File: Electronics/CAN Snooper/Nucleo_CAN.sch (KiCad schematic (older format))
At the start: 35 parts, among them J1 Car Power, J2 CAN Bus, SW1 Reset, T1 12V Iso Test, T10 CAN L Test, T11 CAN Output GND Test, T2 5V Iso Test, T3 9V Test, T4 3.3V Test, T5 CAN PwrSense Test, T6 CAN Tx Test, T7 CAN Rx Test, T8 CAN Input GND Test, T9 CAN H Test, U1 PDS1-S12-S9-M, U2 MCP1702T-5002E/CB, U3 Nucleo_L432KC, U4 ADM3054

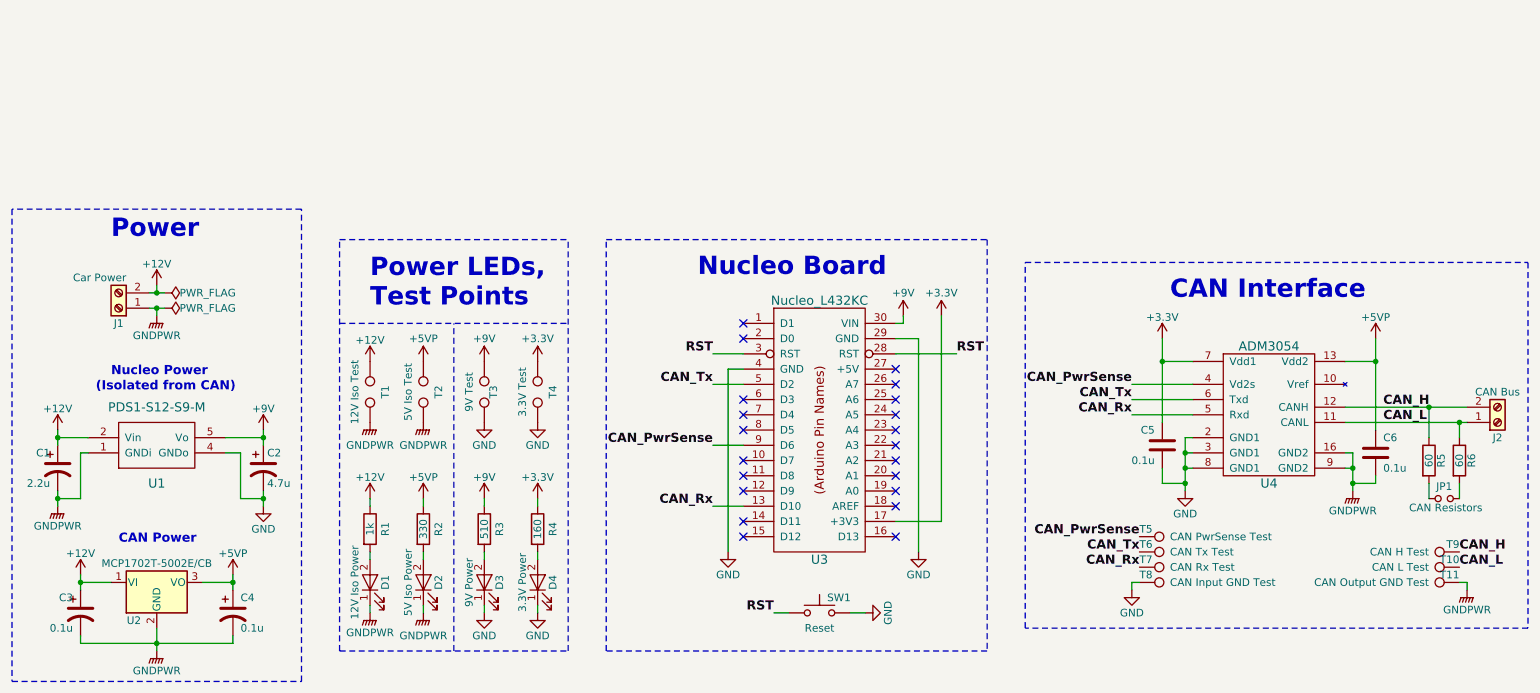
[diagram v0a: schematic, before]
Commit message: CAN Snooper: Schematic: Merge PWR and CAN connectors; bump rev.
In order to facilitate easy power and CAN connection, I've combined
the two into a single connector rather than two separate screw
terminals. Additionally, I've added a duplicate connector to make
chaining CAN connections simple, removing the need for splitters or
radial bus layouts.

I created a schematic symbol for our connector to make sure that we
use a consistent pinout across our designs.

Regenerated Schematic Preview for team members without KiCad.
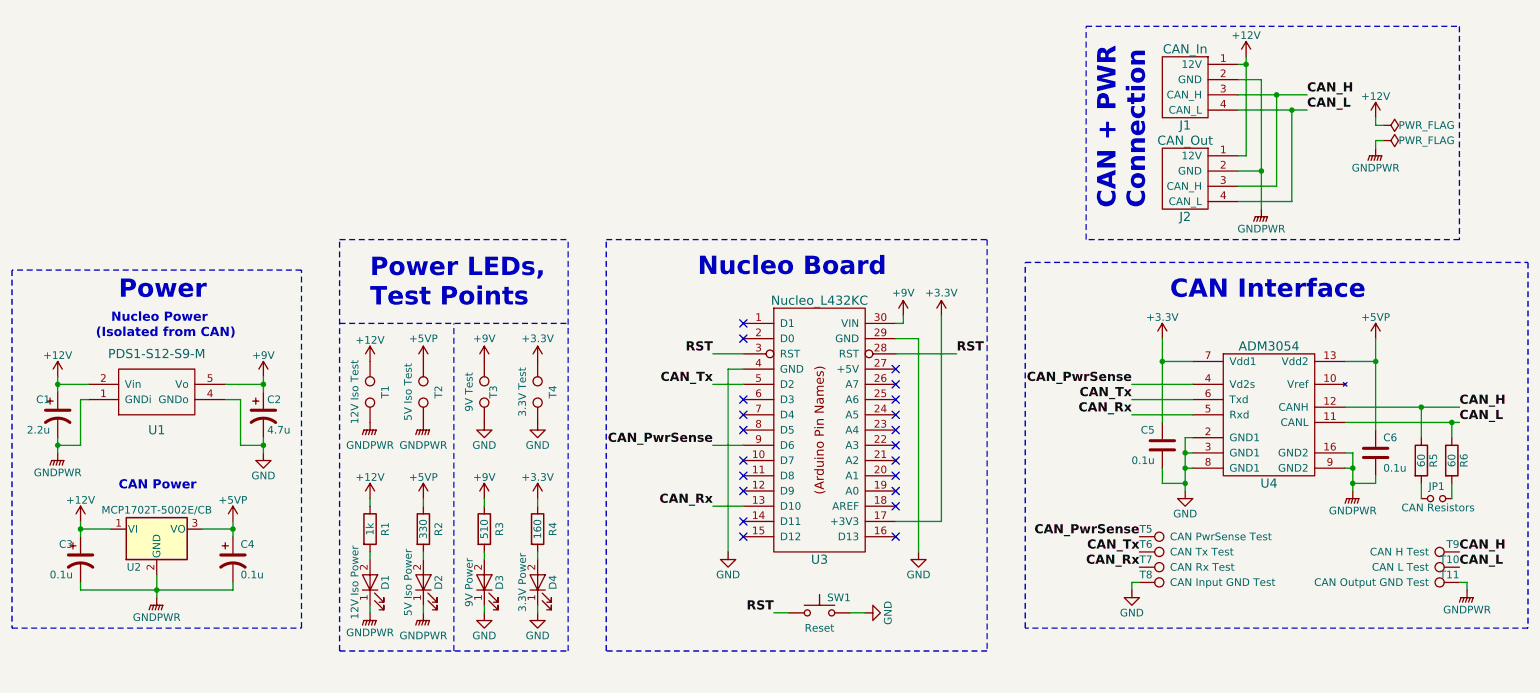
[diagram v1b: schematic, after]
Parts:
- removed J1: Car Power, Connectors_Terminal_Blocks:TerminalBlock_bornier-2_P5.08mm, symbol Screw_Terminal_01x02
- removed J2: CAN Bus, Connectors_Terminal_Blocks:TerminalBlock_bornier-2_P5.08mm, symbol Screw_Terminal_01x02
- added J1: CAN_In, symbol CANConnector
- added J2: CAN_Out, symbol CANConnector
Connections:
- net +12V: now also J1.1 (12V), J2.1 (12V)
- net CAN_H: now also J1.3 (CAN_H), J2.3 (CAN_H)
- net CAN_L: now also J1.4 (CAN_L), J2.4 (CAN_L)
- net GNDPWR: now also J1.2 (GND), J2.2 (GND)
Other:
- note added: "CAN + PWR\nConnection"
- moved on the sheet: C1, C2, C3, C4, JP1, R5, R6, U1, U2

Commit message: CAN Snooper: Added MiniFitJr-4-peg footprint; regenerated netlist.
The connector we plan to use for power and CAN is a Molex Mini-Fit Jr
with 4 pins (Molex calls them "circuits"). The most compact of those
designs uses "pegs" to secure itself to the board.

I designed a footprint for this connector and assigned it to the two
connector footprints we have on the schematic, then regenerated the
netlist.
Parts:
- J1, J2: footprint (none) -> Custom:Molex-MiniFitJr-4-peg
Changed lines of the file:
@@
 F 0 "J1" H 8600 1200 60  0000 C CNN
 F 1 "CAN_In" H 8600 1700 60  0000 C CNN
-F 2 "" H 8750 1750 60  0001 C CNN
+F 2 "Custom:Molex-MiniFitJr-4-peg" H 8750 1750 60  0001 C CNN
 F 3 "" H 8750 1750 60  0001 C CNN
 	1    8600 1450
@@
 F 0 "J2" H 8600 1800 60  0000 C CNN
 F 1 "CAN_Out" H 8600 2300 60  0000 C CNN
-F 2 "" H 8750 2350 60  0001 C CNN
+F 2 "Custom:Molex-MiniFitJr-4-peg" H 8750 2350 60  0001 C CNN
 F 3 "" H 8750 2350 60  0001 C CNN
 	1    8600 2050
